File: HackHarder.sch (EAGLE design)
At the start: 8 parts, among them U1 RFM69HW

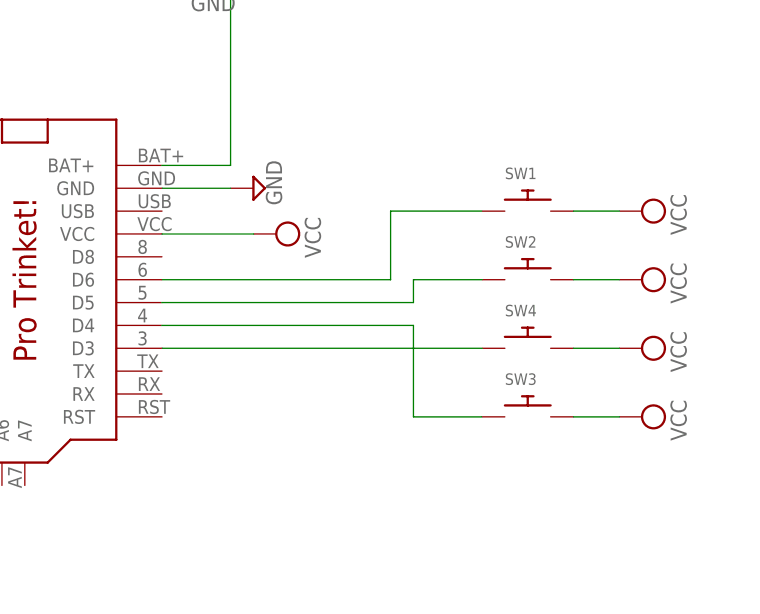
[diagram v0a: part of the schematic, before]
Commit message: Add files via upload
Updated board with smaller footprint
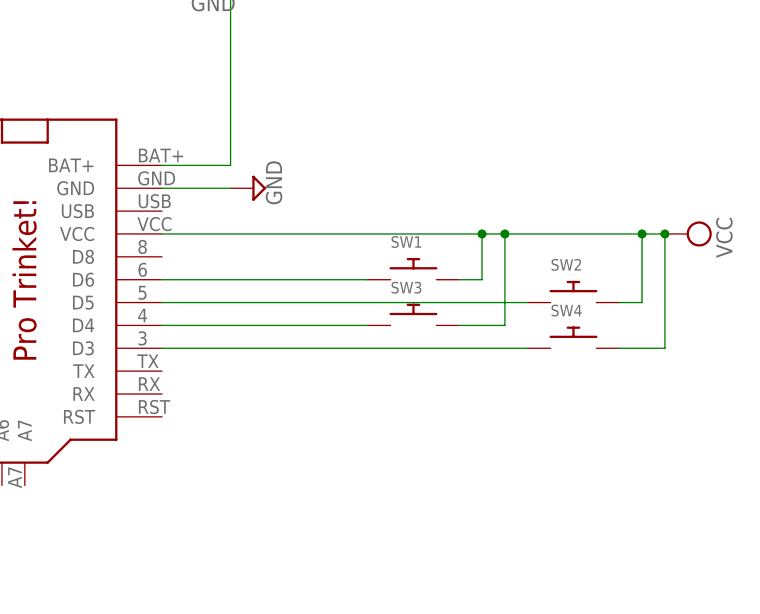
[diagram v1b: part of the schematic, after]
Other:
- moved on the sheet: SW1, SW2, SW3, SW4
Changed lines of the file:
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@@
 <setting verticaltext="up"/>
 </settings>
-<grid distance="0.1" unitdist="inch" unit="inch" style="lines" multiple="1" display="no" altdistance="0.01" altunitdist="inch" altunit="inch"/>
+<grid distance="0.1" unitdist="inch" unit="inch" style="lines" multiple="1" display="yes" altdistance="0.01" altunitdist="inch" altunit="inch"/>
 <layers>
 <layer number="1" name="Top" color="4" fill="1" visible="no" active="no"/>
@@
 <part name="SUPPLY1" library="supply2" deviceset="GND" device=""/>
 <part name="SUPPLY4" library="supply2" deviceset="VCC" device=""/>
-<part name="SUPPLY6" library="supply2" deviceset="VCC" device=""/>
-<part name="SUPPLY7" library="supply2" deviceset="VCC" device=""/>
-<part name="SUPPLY8" library="supply2" deviceset="VCC" device=""/>
-<part name="SUPPLY9" library="supply2" deviceset="VCC" device=""/>
 <part name="U1" library="HopeRF-RFMxx" deviceset="RFM69HW" device=""/>
 <part name="MCU1" library="adafruit" deviceset="PRO_TRINKET" device=""/>
@@
 <part name="SUPPLY3" library="supply2" deviceset="GND" device=""/>
 <part name="SUPPLY10" library="supply2" deviceset="VCC" device=""/>
+<part name="SUPPLY5" library="supply2" deviceset="VCC" device=""/>
+<part name="SUPPLY11" library="supply2" deviceset="GND" device=""/>
+<part name="SW1" library="adafruit" deviceset="SWITCH_PUSHBUTTON" device="EVQ-PE"/>
 <part name="SW2" library="adafruit" deviceset="SWITCH_PUSHBUTTON" device="EVQ-PE"/>
-<part name="SW1" library="adafruit" deviceset="SWITCH_PUSHBUTTON" device="EVQ-PE"/>
 <part name="SW3" library="adafruit" deviceset="SWITCH_PUSHBUTTON" device="EVQ-PE"/>
 <part name="SW4" library="adafruit" deviceset="SWITCH_PUSHBUTTON" device="EVQ-PE"/>
-<part name="SUPPLY5" library="supply2" deviceset="VCC" device=""/>
-<part name="SUPPLY11" library="supply2" deviceset="GND" device=""/>
 </parts>
 <sheets>
@@
 <instance part="CN1" gate="G$1" x="48.26" y="91.44" rot="R90"/>
 <instance part="SUPPLY1" gate="GND" x="45.72" y="78.74"/>
-<instance part="SUPPLY4" gate="G$1" x="53.34" y="50.8" rot="R270"/>
-<instance part="SUPPLY6" gate="G$1" x="93.98" y="45.72" rot="R270"/>
-<instance part="SUPPLY7" gate="G$1" x="93.98" y="53.34" rot="R270"/>
-<instance part="SUPPLY8" gate="G$1" x="93.98" y="30.48" rot="R270"/>
-<instance part="SUPPLY9" gate="G$1" x="93.98" y="38.1" rot="R270"/>
+<instance part="SUPPLY4" gate="G$1" x="99.06" y="50.8" rot="R270"/>
 <instance part="U1" gate="G$1" x="-33.02" y="53.34" rot="R180"/>
 <instance part="MCU1" gate="G$1" x="25.4" y="45.72"/>
@@
 <instance part="SUPPLY3" gate="GND" x="-35.56" y="7.62"/>
 <instance part="SUPPLY10" gate="G$1" x="-38.1" y="15.24" rot="R180"/>
-<instance part="SW2" gate="G$1" x="81.28" y="45.72"/>
-<instance part="SW1" gate="G$1" x="81.28" y="53.34"/>
-<instance part="SW3" gate="G$1" x="81.28" y="30.48"/>
-<instance part="SW4" gate="G$1" x="81.28" y="38.1"/>
 <instance part="SUPPLY5" gate="G$1" x="-7.62" y="45.72" rot="R270"/>
 <instance part="SUPPLY11" gate="GND" x="-7.62" y="60.96" rot="R90"/>
+<instance part="SW1" gate="G$1" x="68.58" y="45.72"/>
+<instance part="SW2" gate="G$1" x="86.36" y="43.18"/>
+<instance part="SW3" gate="G$1" x="68.58" y="40.64"/>
+<instance part="SW4" gate="G$1" x="86.36" y="38.1"/>
 </instances>
 <busses>
@@
 <pinref part="SUPPLY4" gate="G$1" pin="VCC"/>
 <pinref part="MCU1" gate="G$1" pin="VCC"/>
-<wire x1="50.8" y1="50.8" x2="40.64" y2="50.8" width="0.1524" layer="91"/>
+<wire x1="96.52" y1="50.8" x2="93.98" y2="50.8" width="0.1524" layer="91"/>
+<pinref part="SW1" gate="G$1" pin="P$2"/>
+<wire x1="93.98" y1="50.8" x2="78.74" y2="50.8" width="0.1524" layer="91"/>
+<wire x1="78.74" y1="50.8" x2="76.2" y2="50.8" width="0.1524" layer="91"/>
+<wire x1="76.2" y1="50.8" x2="40.64" y2="50.8" width="0.1524" layer="91"/>
+<wire x1="73.66" y1="45.72" x2="76.2" y2="45.72" width="0.1524" layer="91"/>
+<wire x1="76.2" y1="45.72" x2="76.2" y2="50.8" width="0.1524" layer="91"/>
+<junction x="76.2" y="50.8"/>
+<pinref part="SW3" gate="G$1" pin="P$2"/>
+<wire x1="73.66" y1="40.64" x2="78.74" y2="40.64" width="0.1524" layer="91"/>
+<wire x1="78.74" y1="40.64" x2="78.74" y2="50.8" width="0.1524" layer="91"/>
+<junction x="78.74" y="50.8"/>
+<pinref part="SW2" gate="G$1" pin="P$2"/>
+<wire x1="91.44" y1="43.18" x2="93.98" y2="43.18" width="0.1524" layer="91"/>
+<wire x1="93.98" y1="43.18" x2="93.98" y2="50.8" width="0.1524" layer="91"/>
+<junction x="93.98" y="50.8"/>
+<pinref part="SW4" gate="G$1" pin="P$2"/>
+<wire x1="91.44" y1="38.1" x2="96.52" y2="38.1" width="0.1524" layer="91"/>
+<wire x1="96.52" y1="38.1" x2="96.52" y2="50.8" width="0.1524" layer="91"/>
+<junction x="96.52" y="50.8"/>
 </segment>
 <segment>
@@
 <pinref part="SUPPLY5" gate="G$1" pin="VCC"/>
 <wire x1="-15.24" y1="45.72" x2="-10.16" y2="45.72" width="0.1524" layer="91"/>
-</segment>
-<segment>
-<pinref part="SW3" gate="G$1" pin="P$2"/>
-<pinref part="SUPPLY8" gate="G$1" pin="VCC"/>
-<wire x1="86.36" y1="30.48" x2="91.44" y2="30.48" width="0.1524" layer="91"/>
-</segment>
-<segment>
-<pinref part="SW1" gate="G$1" pin="P$2"/>
-<pinref part="SUPPLY7" gate="G$1" pin="VCC"/>
-<wire x1="86.36" y1="53.34" x2="91.44" y2="53.34" width="0.1524" layer="91"/>
-</segment>
-<segment>
-<pinref part="SW2" gate="G$1" pin="P$2"/>
-<pinref part="SUPPLY6" gate="G$1" pin="VCC"/>
-<wire x1="86.36" y1="45.72" x2="91.44" y2="45.72" width="0.1524" layer="91"/>
-</segment>
-<segment>
-<pinref part="SW4" gate="G$1" pin="P$2"/>
-<pinref part="SUPPLY9" gate="G$1" pin="VCC"/>
-<wire x1="86.36" y1="38.1" x2="91.44" y2="38.1" width="0.1524" layer="91"/>
 </segment>
 </net>
@@
 <segment>
 <pinref part="MCU1" gate="G$1" pin="D6"/>
-<wire x1="40.64" y1="45.72" x2="66.04" y2="45.72" width="0.1524" layer="91"/>
-<wire x1="66.04" y1="45.72" x2="66.04" y2="53.34" width="0.1524" layer="91"/>
 <pinref part="SW1" gate="G$1" pin="P$1"/>
-<wire x1="66.04" y1="53.34" x2="76.2" y2="53.34" width="0.1524" layer="91"/>
+<wire x1="40.64" y1="45.72" x2="63.5" y2="45.72" width="0.1524" layer="91"/>
 </segment>
 </net>
@@
 <segment>
 <pinref part="MCU1" gate="G$1" pin="D5"/>
-<wire x1="40.64" y1="43.18" x2="68.58" y2="43.18" width="0.1524" layer="91"/>
-<wire x1="68.58" y1="43.18" x2="68.58" y2="45.72" width="0.1524" layer="91"/>
 <pinref part="SW2" gate="G$1" pin="P$1"/>
-<wire x1="68.58" y1="45.72" x2="76.2" y2="45.72" width="0.1524" layer="91"/>
-</segment>
-</net>
-<net name="N$9" class="0">
-<segment>
+<wire x1="40.64" y1="43.18" x2="81.28" y2="43.18" width="0.1524" layer="91"/>
+</segment>
+</net>
+<net name="N$14" class="0">
+<segment>
+<pinref part="MCU1" gate="G$1" pin="D4"/>
+<pinref part="SW3" gate="G$1" pin="P$1"/>
+<wire x1="40.64" y1="40.64" x2="63.5" y2="40.64" width="0.1524" layer="91"/>
+</segment>
+</net>
+<net name="N$15" class="0">
+<segment>
+<pinref part="MCU1" gate="G$1" pin="D3"/>
 <pinref part="SW4" gate="G$1" pin="P$1"/>
-<pinref part="MCU1" gate="G$1" pin="D3"/>
-<wire x1="76.2" y1="38.1" x2="40.64" y2="38.1" width="0.1524" layer="91"/>
-</segment>
-</net>
-<net name="N$11" class="0">
-<segment>
-<pinref part="MCU1" gate="G$1" pin="D4"/>
-<wire x1="40.64" y1="40.64" x2="68.58" y2="40.64" width="0.1524" layer="91"/>
-<wire x1="68.58" y1="40.64" x2="68.58" y2="30.48" width="0.1524" layer="91"/>
-<pinref part="SW3" gate="G$1" pin="P$1"/>
-<wire x1="68.58" y1="30.48" x2="76.2" y2="30.48" width="0.1524" layer="91"/>
-</segment>
-</net>
+<wire x1="40.64" y1="38.1" x2="81.28" y2="38.1" width="0.1524" layer="91"/>
+</segment>
+</net>

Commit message: Add files via upload
Now with serial breakout!  I'm not sure that the footprint for the radio is correct - need to double-check the pintout on the module spec sheet...
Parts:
- added SERIAL: (no value), adafruit:PINHD-1X3
- renumbered SV1 to OLED
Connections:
- new net N$16: MCU1.TX, SERIAL.1
- new net N$17: MCU1.RX, SERIAL.2
- net G$1: now also SERIAL.3
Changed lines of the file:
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@@
 <part name="U1" library="HopeRF-RFMxx" deviceset="RFM69HW" device=""/>
 <part name="MCU1" library="adafruit" deviceset="PRO_TRINKET" device=""/>
-<part name="SV1" library="con-lstb" deviceset="MA04-1" device=""/>
+<part name="OLED" library="con-lstb" deviceset="MA04-1" device=""/>
 <part name="SUPPLY2" library="supply2" deviceset="GND" device=""/>
 <part name="SUPPLY3" library="supply2" deviceset="GND" device=""/>
 <part name="SUPPLY10" library="supply2" deviceset="VCC" device=""/>
-<part name="SUPPLY5" library="supply2" deviceset="VCC" device=""/>
 <part name="SUPPLY11" library="supply2" deviceset="GND" device=""/>
 <part name="SW1" library="adafruit" deviceset="SWITCH_PUSHBUTTON" device="EVQ-PE"/>
@@
 <part name="SW3" library="adafruit" deviceset="SWITCH_PUSHBUTTON" device="EVQ-PE"/>
 <part name="SW4" library="adafruit" deviceset="SWITCH_PUSHBUTTON" device="EVQ-PE"/>
+<part name="SERIAL" library="adafruit" deviceset="PINHD-1X3" device=""/>
 </parts>
 <sheets>
@@
 <instance part="U1" gate="G$1" x="-33.02" y="53.34" rot="R180"/>
 <instance part="MCU1" gate="G$1" x="25.4" y="45.72"/>
-<instance part="SV1" gate="1" x="-33.02" y="30.48" rot="R270"/>
+<instance part="OLED" gate="1" x="-33.02" y="30.48" rot="R270"/>
 <instance part="SUPPLY2" gate="GND" x="50.8" y="55.88" rot="R90"/>
 <instance part="SUPPLY3" gate="GND" x="-35.56" y="7.62"/>
 <instance part="SUPPLY10" gate="G$1" x="-38.1" y="15.24" rot="R180"/>
-<instance part="SUPPLY5" gate="G$1" x="-7.62" y="45.72" rot="R270"/>
 <instance part="SUPPLY11" gate="GND" x="-7.62" y="60.96" rot="R90"/>
 <instance part="SW1" gate="G$1" x="68.58" y="45.72"/>
@@
 <instance part="SW3" gate="G$1" x="68.58" y="40.64"/>
 <instance part="SW4" gate="G$1" x="86.36" y="38.1"/>
+<instance part="SERIAL" gate="A" x="68.58" y="25.4"/>
 </instances>
 <busses>
@@
 </segment>
 <segment>
-<pinref part="SV1" gate="1" pin="2"/>
+<pinref part="OLED" gate="1" pin="2"/>
 <pinref part="SUPPLY3" gate="GND" pin="GND"/>
-<wire x1="-35.56" y1="22.86" x2="-35.56" y2="10.16" width="0.1524" layer="91"/>
+<wire x1="-35.56" y1="22.86" x2="-35.56" y2="12.7" width="0.1524" layer="91"/>
+<wire x1="-35.56" y1="12.7" x2="-35.56" y2="10.16" width="0.1524" layer="91"/>
+<wire x1="-35.56" y1="12.7" x2="50.8" y2="12.7" width="0.1524" layer="91"/>
+<wire x1="50.8" y1="12.7" x2="50.8" y2="22.86" width="0.1524" layer="91"/>
+<junction x="-35.56" y="12.7"/>
+<pinref part="SERIAL" gate="A" pin="3"/>
+<wire x1="50.8" y1="22.86" x2="66.04" y2="22.86" width="0.1524" layer="91"/>
 </segment>
 <segment>
@@
 <wire x1="96.52" y1="50.8" x2="93.98" y2="50.8" width="0.1524" layer="91"/>
 <pinref part="SW1" gate="G$1" pin="P$2"/>
-<wire x1="93.98" y1="50.8" x2="78.74" y2="50.8" width="0.1524" layer="91"/>
+<wire x1="93.98" y1="50.8" x2="86.36" y2="50.8" width="0.1524" layer="91"/>
+<wire x1="86.36" y1="50.8" x2="78.74" y2="50.8" width="0.1524" layer="91"/>
 <wire x1="78.74" y1="50.8" x2="76.2" y2="50.8" width="0.1524" layer="91"/>
 <wire x1="76.2" y1="50.8" x2="40.64" y2="50.8" width="0.1524" layer="91"/>
@@
 <wire x1="96.52" y1="38.1" x2="96.52" y2="50.8" width="0.1524" layer="91"/>
 <junction x="96.52" y="50.8"/>
-</segment>
-<segment>
-<pinref part="SV1" gate="1" pin="1"/>
+<pinref part="U1" gate="G$1" pin="VCC"/>
+<wire x1="-15.24" y1="45.72" x2="2.54" y2="45.72" width="0.1524" layer="91"/>
+<wire x1="2.54" y1="45.72" x2="2.54" y2="68.58" width="0.1524" layer="91"/>
+<wire x1="2.54" y1="68.58" x2="86.36" y2="68.58" width="0.1524" layer="91"/>
+<wire x1="86.36" y1="68.58" x2="86.36" y2="50.8" width="0.1524" layer="91"/>
+<junction x="86.36" y="50.8"/>
+</segment>
+<segment>
+<pinref part="OLED" gate="1" pin="1"/>
 <pinref part="SUPPLY10" gate="G$1" pin="VCC"/>
 <wire x1="-38.1" y1="17.78" x2="-38.1" y2="22.86" width="0.1524" layer="91"/>
-</segment>
-<segment>
-<pinref part="U1" gate="G$1" pin="VCC"/>
-<pinref part="SUPPLY5" gate="G$1" pin="VCC"/>
-<wire x1="-15.24" y1="45.72" x2="-10.16" y2="45.72" width="0.1524" layer="91"/>
 </segment>
 </net>
@@
 <wire x1="10.16" y1="30.48" x2="5.08" y2="30.48" width="0.1524" layer="91"/>
 <wire x1="5.08" y1="30.48" x2="5.08" y2="17.78" width="0.1524" layer="91"/>
-<pinref part="SV1" gate="1" pin="3"/>
+<pinref part="OLED" gate="1" pin="3"/>
 <wire x1="5.08" y1="17.78" x2="-33.02" y2="17.78" width="0.1524" layer="91"/>
 <wire x1="-33.02" y1="17.78" x2="-33.02" y2="22.86" width="0.1524" layer="91"/>
@@
 <wire x1="10.16" y1="33.02" x2="2.54" y2="33.02" width="0.1524" layer="91"/>
 <wire x1="2.54" y1="33.02" x2="2.54" y2="20.32" width="0.1524" layer="91"/>
-<pinref part="SV1" gate="1" pin="4"/>
+<pinref part="OLED" gate="1" pin="4"/>
 <wire x1="2.54" y1="20.32" x2="-30.48" y2="20.32" width="0.1524" layer="91"/>
 <wire x1="-30.48" y1="20.32" x2="-30.48" y2="22.86" width="0.1524" layer="91"/>
@@
 </segment>
 </net>
+<net name="N$16" class="0">
+<segment>
+<pinref part="MCU1" gate="G$1" pin="TX"/>
+<wire x1="40.64" y1="35.56" x2="53.34" y2="35.56" width="0.1524" layer="91"/>
+<wire x1="53.34" y1="35.56" x2="53.34" y2="27.94" width="0.1524" layer="91"/>
+<pinref part="SERIAL" gate="A" pin="1"/>
+<wire x1="53.34" y1="27.94" x2="66.04" y2="27.94" width="0.1524" layer="91"/>
+</segment>
+</net>
+<net name="N$17" class="0">
+<segment>
+<pinref part="MCU1" gate="G$1" pin="RX"/>
+<wire x1="40.64" y1="33.02" x2="50.8" y2="33.02" width="0.1524" layer="91"/>
+<wire x1="50.8" y1="33.02" x2="50.8" y2="25.4" width="0.1524" layer="91"/>
+<pinref part="SERIAL" gate="A" pin="2"/>
+<wire x1="50.8" y1="25.4" x2="66.04" y2="25.4" width="0.1524" layer="91"/>
+</segment>
+</net>
